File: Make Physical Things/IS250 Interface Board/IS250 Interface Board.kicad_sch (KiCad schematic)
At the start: 8 parts, among them J1 24_Pin_Reorg, J2 16_Pin, J3 Barrel_Jack, J4 XT60-M, SW1 SW_SPST, SW2 SW_MEC_5G, SW6 SW_MEC_5G

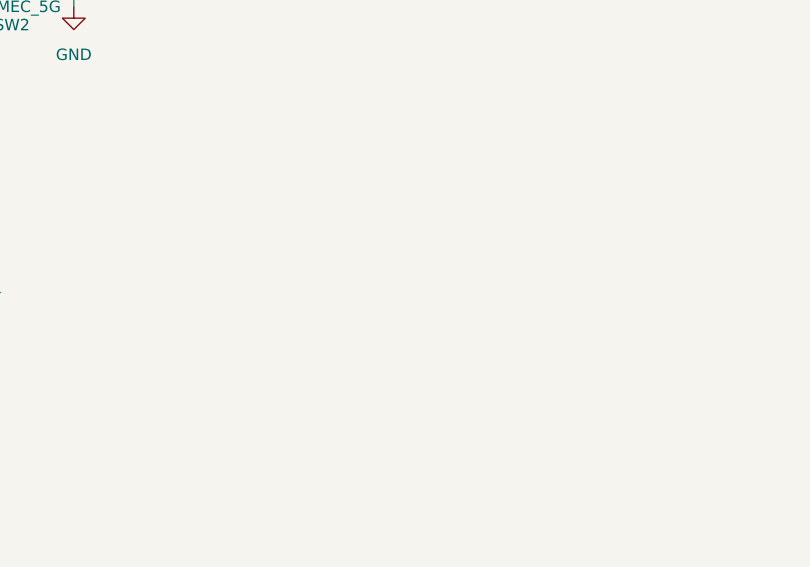
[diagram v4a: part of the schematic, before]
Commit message: Added Power LED's and PCB foundation
Added LED's to indicate both 12v and 5v power to the board, and begun work on the PCB
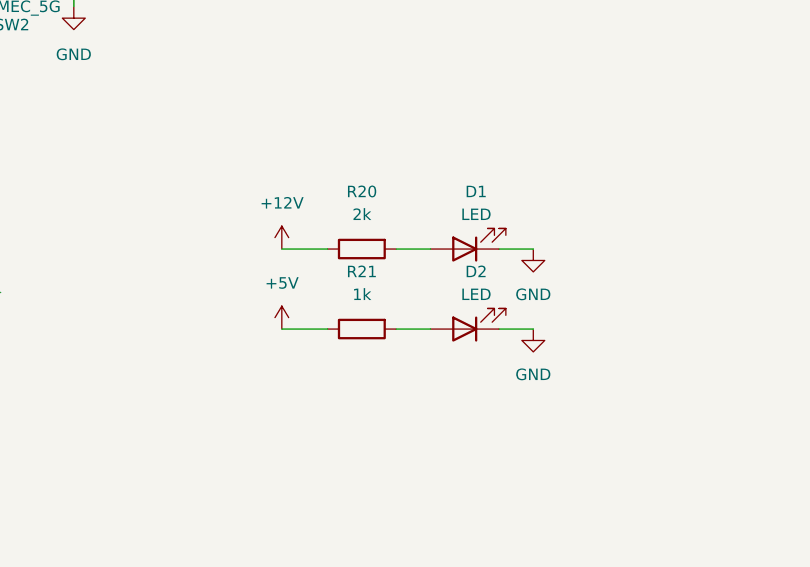
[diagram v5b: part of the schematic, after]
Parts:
- added D1, D2: LED, LED_THT:LED_D5.0mm, symbol Device:LED
- added R20: 2k, Resistor_THT:R_Axial_DIN0207_L6.3mm_D2.5mm_P10.16mm_Horizontal, symbol Device:R
- added R21: 1k, Resistor_THT:R_Axial_DIN0207_L6.3mm_D2.5mm_P10.16mm_Horizontal, symbol Device:R
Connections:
- net +12V: now also R20.1
- net +5V: now also R21.1
- net GND: now also D1.1 (K), D2.1 (K)
- new net: D2.2 (A), R21.2
- new net: D1.2 (A), R20.2
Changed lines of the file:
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@@
+    (stroke (width 0) (type default) (color 0 0 0 0))
+  )
+  (wire (pts (xy 231.14 123.19) (xy 234.95 123.19))
     (stroke (width 0) (type default) (color 0 0 0 0))
   )
@@
     (stroke (width 0) (type default) (color 0 0 0 0))
   )
+  (wire (pts (xy 219.71 123.19) (xy 223.52 123.19))
+    (stroke (width 0) (type default) (color 0 0 0 0))
+  )
   (wire (pts (xy 165.354 80.772) (xy 166.878 80.772))
     (stroke (width 0) (type default) (color 0 0 0 0))
@@
     (stroke (width 0) (type default) (color 0 0 0 0))
   )
+  (wire (pts (xy 231.14 114.3) (xy 234.95 114.3))
+    (stroke (width 0) (type default) (color 0 0 0 0))
+  )
   (wire (pts (xy 106.68 60.452) (xy 116.586 60.452))
     (stroke (width 0) (type default) (color 0 0 0 0))
@@
     (stroke (width 0) (type default) (color 0 0 0 0))
   )
+  (wire (pts (xy 207.01 123.19) (xy 212.09 123.19))
+    (stroke (width 0) (type default) (color 0 0 0 0))
+  )
   (wire (pts (xy 182.118 85.852) (xy 183.896 85.852))
     (stroke (width 0) (type default) (color 0 0 0 0))
@@
     (stroke (width 0) (type default) (color 0 0 0 0))
   )
+  (wire (pts (xy 219.71 114.3) (xy 223.52 114.3))
+    (stroke (width 0) (type default) (color 0 0 0 0))
+  )
   (wire (pts (xy 236.22 76.2) (xy 246.38 76.2))
     (stroke (width 0) (type default) (color 0 0 0 0))
@@
   )
   (wire (pts (xy 106.68 137.16) (xy 99.06 137.16))
+    (stroke (width 0) (type default) (color 0 0 0 0))
+  )
+  (wire (pts (xy 207.01 114.3) (xy 212.09 114.3))
     (stroke (width 0) (type default) (color 0 0 0 0))
   )
@@
     (pin "2")
     (pin "4")
+  )
+  (symbol (lib_id "Device:R") (at 215.9 123.19 90) (mirror x) (unit 1)
+    (in_bom yes) (on_board yes) (fields_autoplaced)
+    (property "Reference" "R21" (id 0) (at 215.9 116.84 90))
+    (property "Value" "1k" (id 1) (at 215.9 119.38 90))
+    (property "Footprint" "Resistor_THT:R_Axial_DIN0207_L6.3mm_D2.5mm_P10.16mm_Horizontal" (id 2) (at 215.9 121.412 90)
+      (effects (font (size 1.27 1.27)) hide)
+    )
+    (property "Datasheet" "~" (id 3) (at 215.9 123.19 0)
+      (effects (font (size 1.27 1.27)) hide)
+    )
+    (pin "1")
+    (pin "2")
   )
   (symbol (lib_id "power:+12V") (at 256.54 31.75 0) (unit 1)
@@
     (pin "VIN")
   )
+  (symbol (lib_id "power:GND") (at 234.95 114.3 0) (unit 1)
+    (in_bom yes) (on_board yes) (fields_autoplaced)
+    (property "Reference" "#PWR0137" (id 0) (at 234.95 120.65 0)
+      (effects (font (size 1.27 1.27)) hide)
+    )
+    (property "Value" "GND" (id 1) (at 234.95 119.38 0))
+    (property "Footprint" "" (id 2) (at 234.95 114.3 0)
+      (effects (font (size 1.27 1.27)) hide)
+    )
+    (property "Datasheet" "" (id 3) (at 234.95 114.3 0)
+      (effects (font (size 1.27 1.27)) hide)
+    )
+    (pin "1")
+  )
+  (symbol (lib_id "Device:LED") (at 227.33 123.19 180) (unit 1)
+    (in_bom yes) (on_board yes)
+    (property "Reference" "D2" (id 0) (at 228.6 116.84 0))
+    (property "Value" "LED" (id 1) (at 228.6 119.38 0))
+    (property "Footprint" "LED_THT:LED_D5.0mm" (id 2) (at 227.33 123.19 0)
+      (effects (font (size 1.27 1.27)) hide)
+    )
+    (property "Datasheet" "~" (id 3) (at 227.33 123.19 0)
+      (effects (font (size 1.27 1.27)) hide)
+    )
+    (pin "1")
+    (pin "2")
+  )
   (symbol (lib_id "Switch:SW_SPST") (at 134.874 80.772 0) (mirror y) (unit 1)
     (in_bom yes) (on_board yes)
@@
     (pin "1")
   )
+  (symbol (lib_id "Device:LED") (at 227.33 114.3 180) (unit 1)
+    (in_bom yes) (on_board yes)
+    (property "Reference" "D1" (id 0) (at 228.6 107.95 0))
+    (property "Value" "LED" (id 1) (at 228.6 110.49 0))
+    (property "Footprint" "LED_THT:LED_D5.0mm" (id 2) (at 227.33 114.3 0)
+      (effects (font (size 1.27 1.27)) hide)
+    )
+    (property "Datasheet" "~" (id 3) (at 227.33 114.3 0)
+      (effects (font (size 1.27 1.27)) hide)
+    )
+    (pin "1")
+    (pin "2")
+  )
   (symbol (lib_id "power:GND") (at 256.54 36.83 0) (unit 1)
     (in_bom yes) (on_board yes) (fields_autoplaced)
@@
     (pin "1")
   )
+  (symbol (lib_id "power:+12V") (at 207.01 114.3 0) (unit 1)
+    (in_bom yes) (on_board yes) (fields_autoplaced)
+    (property "Reference" "#PWR0138" (id 0) (at 207.01 118.11 0)
+      (effects (font (size 1.27 1.27)) hide)
+    )
+    (property "Value" "+12V" (id 1) (at 207.01 109.22 0))
+    (property "Footprint" "" (id 2) (at 207.01 114.3 0)
+      (effects (font (size 1.27 1.27)) hide)
+    )
+    (property "Datasheet" "" (id 3) (at 207.01 114.3 0)
+      (effects (font (size 1.27 1.27)) hide)
+    )
+    (pin "1")
+  )
+  (symbol (lib_id "power:GND") (at 234.95 123.19 0) (unit 1)
+    (in_bom yes) (on_board yes) (fields_autoplaced)
+    (property "Reference" "#PWR0136" (id 0) (at 234.95 129.54 0)
+      (effects (font (size 1.27 1.27)) hide)
+    )
+    (property "Value" "GND" (id 1) (at 234.95 128.27 0))
+    (property "Footprint" "" (id 2) (at 234.95 123.19 0)
+      (effects (font (size 1.27 1.27)) hide)
+    )
+    (property "Datasheet" "" (id 3) (at 234.95 123.19 0)
+      (effects (font (size 1.27 1.27)) hide)
+    )
+    (pin "1")
+  )
   (symbol (lib_id "power:+12V") (at 256.54 50.8 0) (unit 1)
     (in_bom yes) (on_board yes) (fields_autoplaced)
@@
     )
     (property "Datasheet" "~" (id 3) (at 265.43 35.306 0)
+      (effects (font (size 1.27 1.27)) hide)
+    )
+    (pin "1")
+    (pin "2")
+  )
+  (symbol (lib_id "Device:R") (at 215.9 114.3 90) (mirror x) (unit 1)
+    (in_bom yes) (on_board yes) (fields_autoplaced)
+    (property "Reference" "R20" (id 0) (at 215.9 107.95 90))
+    (property "Value" "2k" (id 1) (at 215.9 110.49 90))
+    (property "Footprint" "Resistor_THT:R_Axial_DIN0207_L6.3mm_D2.5mm_P10.16mm_Horizontal" (id 2) (at 215.9 112.522 90)
+      (effects (font (size 1.27 1.27)) hide)
+    )
+    (property "Datasheet" "~" (id 3) (at 215.9 114.3 0)
       (effects (font (size 1.27 1.27)) hide)
     )
@@
     (pin "1")
   )
+  (symbol (lib_id "power:+5V") (at 207.01 123.19 0) (unit 1)
+    (in_bom yes) (on_board yes) (fields_autoplaced)
+    (property "Reference" "#PWR0139" (id 0) (at 207.01 127 0)
+      (effects (font (size 1.27 1.27)) hide)
+    )
+    (property "Value" "+5V" (id 1) (at 207.01 118.11 0))
+    (property "Footprint" "" (id 2) (at 207.01 123.19 0)
+      (effects (font (size 1.27 1.27)) hide)
+    )
+    (property "Datasheet" "" (id 3) (at 207.01 123.19 0)
+      (effects (font (size 1.27 1.27)) hide)
+    )
+    (pin "1")
+  )
   (symbol (lib_id "IS250 Interface Board:16_Pin") (at 152.908 125.476 0) (unit 1)
     (in_bom yes) (on_board yes) (fields_autoplaced)
@@
       (reference "#PWR0135") (unit 1) (value "GND") (footprint "")
     )
+    (path "/843d6cba-af67-4c7f-b5e9-cf7befa87955"
+      (reference "#PWR0136") (unit 1) (value "GND") (footprint "")
+    )
+    (path "/59a8482b-7745-4910-ac9c-7ed8f4c6a0a8"
+      (reference "#PWR0137") (unit 1) (value "GND") (footprint "")
+    )
+    (path "/77458c1b-b137-42d4-b580-9525713d2496"
+      (reference "#PWR0138") (unit 1) (value "+12V") (footprint "")
+    )
+    (path "/cd0e6fba-3b83-4dde-b854-0c0176da4c7e"
+      (reference "#PWR0139") (unit 1) (value "+5V") (footprint "")
+    )
+    (path "/720eca04-a3da-40f8-b2be-6a627090481e"
+      (reference "D1") (unit 1) (value "LED") (footprint "LED_THT:LED_D5.0mm")
+    )
+    (path "/5f4249b1-0bb8-4208-85ab-d3af54e1a867"
+      (reference "D2") (unit 1) (value "LED") (footprint "LED_THT:LED_D5.0mm")
+    )
     (path "/b4ad7ea6-c60f-4c23-983b-e568869cc5ae"
       (reference "J1") (unit 1) (value "24_Pin_Reorg") (footprint "IS250 Interface Board:24Pin")
@@
       (reference "R19") (unit 1) (value "100") (footprint "Resistor_THT:R_Axial_DIN0207_L6.3mm_D2.5mm_P10.16mm_Horizontal")
     )
+    (path "/9e2fcea5-3788-4bcd-9a3c-1e7ac098b115"
+      (reference "R20") (unit 1) (value "2k") (footprint "Resistor_THT:R_Axial_DIN0207_L6.3mm_D2.5mm_P10.16mm_Horizontal")
+    )
+    (path "/14cf7aad-a489-43f3-9a25-c7704f1bc30c"
+      (reference "R21") (unit 1) (value "1k") (footprint "Resistor_THT:R_Axial_DIN0207_L6.3mm_D2.5mm_P10.16mm_Horizontal")
+    )
     (path "/befd90f1-e350-4c6b-9126-156e7cfd54fd/f532fa97-167c-4bca-bcaf-4a540362fc1c"

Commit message: More PCB Layout
PCB laid out further, and just requires routing and silkscreen.
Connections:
- net GND: now also SW2.4 (B); no longer SW2.1 (A)
- new net: J1.20 (DISP-SW), SW2.1 (A), SW2.2 (A)
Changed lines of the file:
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@@
     (pin "P")
   )
-  (symbol (lib_id "Switch:SW_MEC_5G") (at 177.038 85.852 0) (mirror y) (unit 1)
+  (symbol (lib_id "Switch:SW_MEC_5G") (at 177.038 85.852 0) (unit 1)
     (in_bom yes) (on_board yes)
     (property "Reference" "SW2" (id 0) (at 177.038 89.408 0))
@@
     )
     (pin "1")
-    (pin "3")
+    (pin "2")
     (pin "2")
     (pin "4")

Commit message: PCB Layout Finalised
Finalised the layout, routing and silkscreen still to be completed.
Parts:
- added J5: Conn_01x02, Connector_PinHeader_2.54mm:PinHeader_1x02_P2.54mm_Vertical, symbol Connector_Generic:Conn_01x02
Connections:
- net GND: now also XA1.GND6 (GND), J5.2 (Pin_2)
- net at J1.20 (DISP-SW), SW2.1 (A), SW2.2 (A): now also J5.1 (Pin_1)
- no-connect marks 98 -> 97
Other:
- note added: "Power Indicators"
- moved on the sheet: D1, D2, J1, J2, J3, J4, R20, R21, SW1, SW2
